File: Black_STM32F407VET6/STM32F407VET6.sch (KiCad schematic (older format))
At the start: 99 parts, among them J1 T0, J10 - HotBed +, J11 Heater0, J12 X-, J13 Y-, J14 Z-, J15 Z+, J16 USB_B, J17 LeftSpi, J18 EXTRAPINS, J19 12Vinput, J2 T1, J20 5VOut, J23 EXP2, J24 LCD2004, J25 Bottom, J26 Right, J28 LIGHTS, J29 Z, J3 TB, J30 Z, J38 X, J39 Y, J4 TC, J41 E0, J43 Heater1, J44 COM, J47 I2C, J48 SPI, J49 SPI, J5 + VIN -, J50 SDIO, J51 Servo, J52 Servo, J53 PowerSelect, J54 Power, J55 PD11, J56 Power, J6 Fan3, J7 Fan2, J8 Fan1, J9 Fan0, Q1 BCX70, Q10 BCX70, Q11 BCX70, Q12 IRLR8726PBF, Q13 IRLR8726PBF, Q14 IRLR8726PBF, Q2 BCX70, Q3 BCX70, Q4 IRLML0030TRPBF, Q5 BCX70, Q6 IRLML0030TRPBF, Q7 IRLML0030TRPBF, Q8 IRLML0030TRPBF, Q9 BCX70, SW1 Boot0, U1 LeftAnalog, U2 Left5V, U3 BuckConvertor, U5 AT24CS01-SSHM

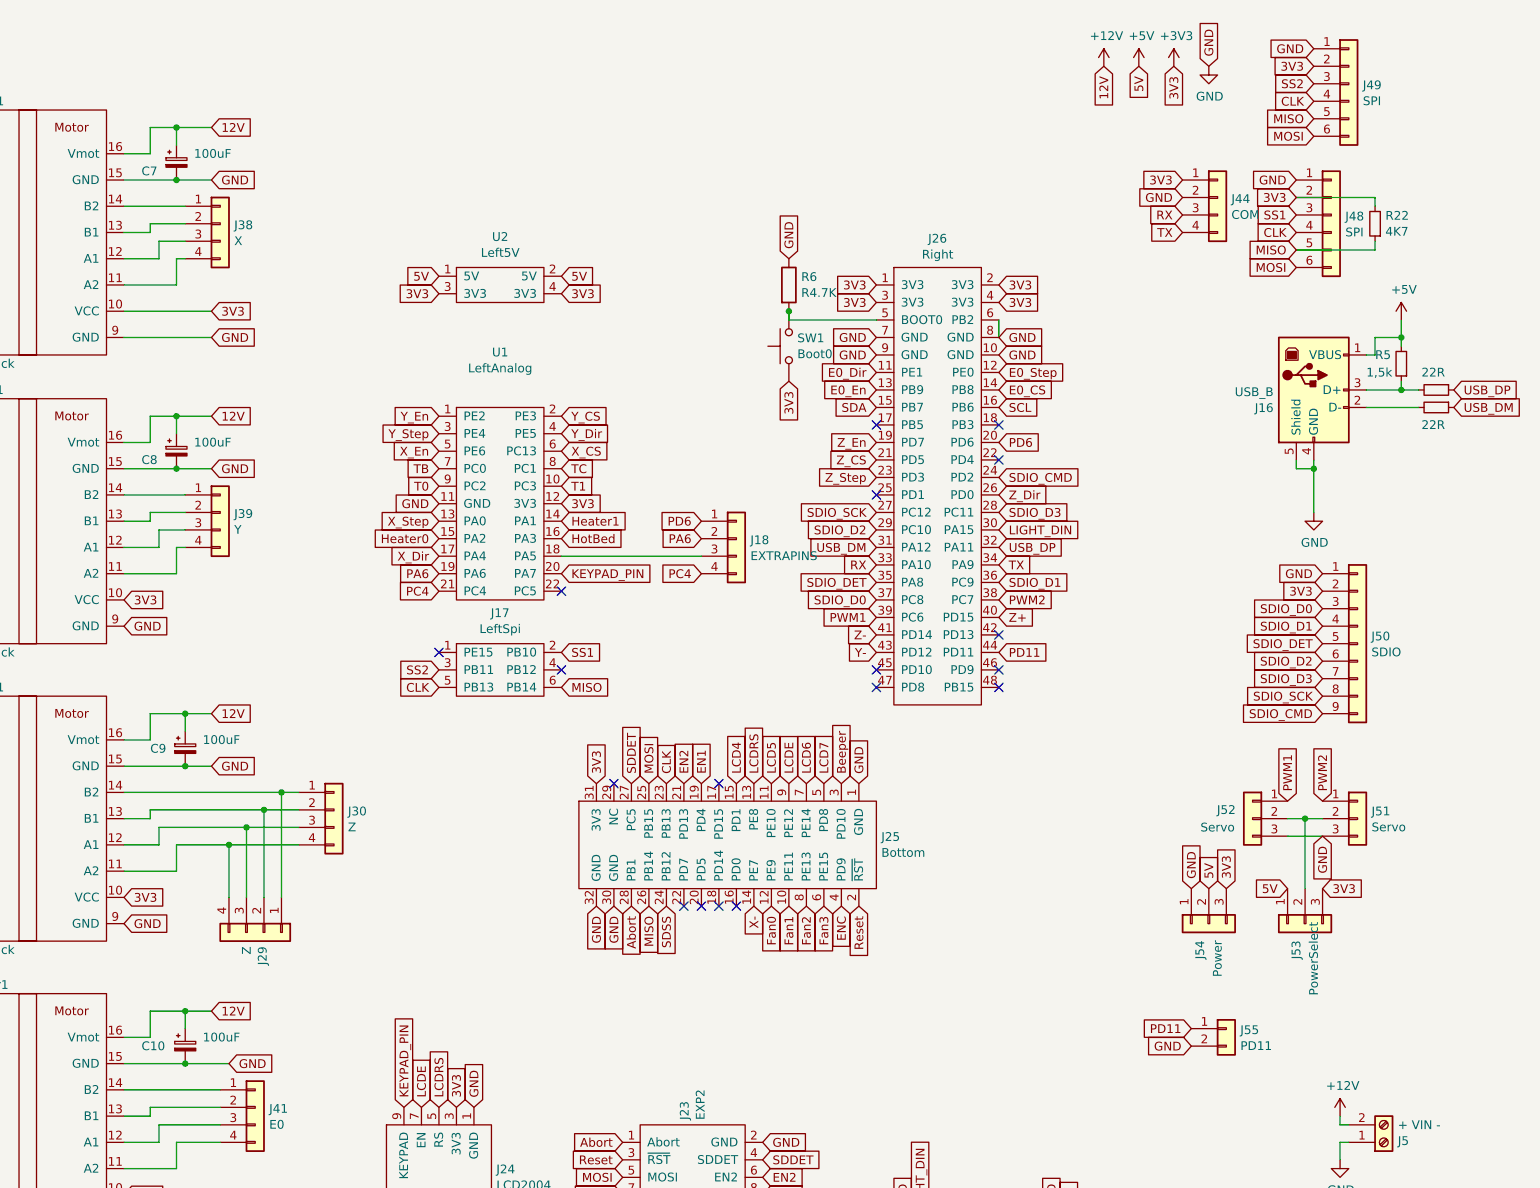
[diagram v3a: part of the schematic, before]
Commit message: Flipped back resistors to the front
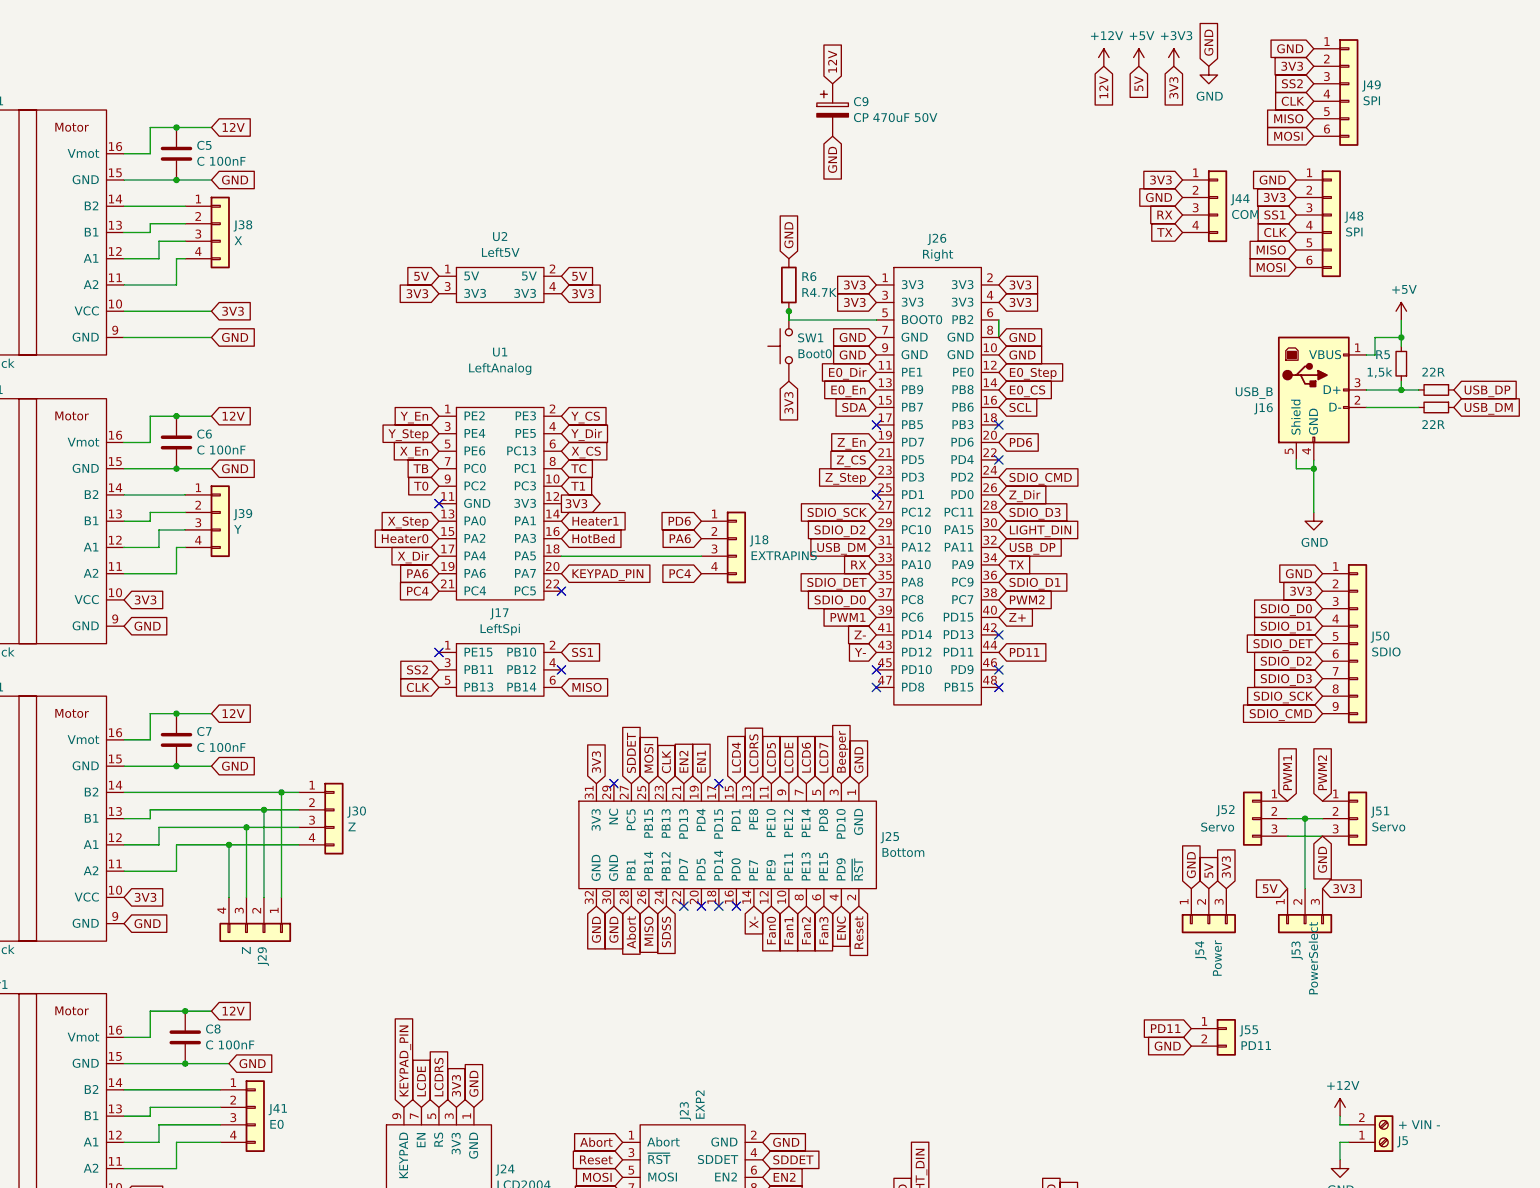
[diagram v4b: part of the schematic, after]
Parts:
- removed C10, C7, C8, C9: 100uF, Capacitor_SMD:CP_Elec_8x6.9, symbol Device:CP_Small
- removed R22: 4K7, Resistor_SMD:R_0603_1608Metric, symbol Device:R_Small
- added C5, C6, C7, C8: C 100nF, Capacitor_THT:C_Disc_D3.4mm_W2.1mm_P2.50mm, symbol Device:C
- added C9: CP 470uF 50V, Capacitor_THT:CP_Radial_D10.0mm_P5.00mm, symbol Device:CP
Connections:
- wire segments 254 -> 246
- no-connect marks 22 -> 23
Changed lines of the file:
@@
 3V3
-$Comp
-L Device:CP_Small C8
-U 1 1 5C4B7C75
-P 8300 3000
-F 0 "C8" H 8100 2950 50  0000 L CNN
-F 1 "100uF" H 8400 3050 50  0000 L CNN
-F 2 "Capacitor_SMD:CP_Elec_8x6.9" H 8300 3000 50  0001 C CNN
-F 3 "~" H 8300 3000 50  0001 C CNN
-	1    8300 3000
-	1    0    0    -1
-$EndComp
-$Comp
-L Device:CP_Small C7
-U 1 1 5C4B6EC9
-P 8300 1350
-F 0 "C7" H 8100 1300 50  0000 L CNN
-F 1 "100uF" H 8400 1400 50  0000 L CNN
-F 2 "Capacitor_SMD:CP_Elec_8x6.9" H 8300 1350 50  0001 C CNN
-F 3 "~" H 8300 1350 50  0001 C CNN
-	1    8300 1350
-	1    0    0    -1
-$EndComp
 $Comp
 L Connector_Generic:Conn_01x04 J39
@@
 Text GLabel 14700 1950 0    50   Input ~ 0
 MOSI
-Wire Wire Line
-	14700 1550 15150 1550
-Wire Wire Line
-	15150 1850 15150 1800
-Wire Wire Line
-	15150 1550 15150 1600
 Text GLabel 14100 5500 1    50   Input ~ 0
 GND
@@
 	1    15000 900
 	1    0    0    -1
-$EndComp
-Wire Wire Line
-	14700 1850 15150 1850
-$Comp
-L Device:R_Small R22
-U 1 1 5C6C524A
-P 15150 1700
-F 0 "R22" H 15091 1654 50  0000 R CNN
-F 1 "4K7" H 15091 1745 50  0000 R CNN
-F 2 "Resistor_SMD:R_0603_1608Metric" H 15150 1700 50  0001 C CNN
-F 3 "~" H 15150 1700 50  0001 C CNN
-	1    15150 1700
-	-1   0    0    1
 $EndComp
 Text GLabel 14700 1650 0    50   Input ~ 0
@@
 Wire Wire Line
 	4300 9450 4550 9450
-$Comp
-L Device:CP_Small C9
-U 1 1 5D30CFC0
-P 8350 4700
-F 0 "C9" H 8150 4700 50  0000 L CNN
-F 1 "100uF" H 8450 4750 50  0000 L CNN
-F 2 "Capacitor_SMD:CP_Elec_8x6.9" H 8350 4700 50  0001 C CNN
-F 3 "~" H 8350 4700 50  0001 C CNN
-	1    8350 4700
-	1    0    0    -1
-$EndComp
 Text GLabel 8000 5550 2    50   Input ~ 0
 3V3
@@
 	1    0    0    -1
 $EndComp
-$Comp
-L Device:CP_Small C10
-U 1 1 5C4B9316
-P 8350 6400
-F 0 "C10" H 8100 6400 50  0000 L CNN
-F 1 "100uF" H 8450 6450 50  0000 L CNN
-F 2 "Capacitor_SMD:CP_Elec_8x6.9" H 8350 6400 50  0001 C CNN
-F 3 "~" H 8350 6400 50  0001 C CNN
-	1    8350 6400
-	1    0    0    -1
-$EndComp
 Text GLabel 8000 7250 2    50   Input ~ 0
 3V3
@@
 	8150 1300 8150 1150
 Wire Wire Line
-	8150 1150 8300 1150
-Wire Wire Line
-	8300 1250 8300 1150
-Connection ~ 8300 1150
-Wire Wire Line
-	8300 1150 8500 1150
-Wire Wire Line
-	8000 1450 8300 1450
-Connection ~ 8300 1450
-Wire Wire Line
-	8300 1450 8500 1450
-Wire Wire Line
 	8000 1600 8350 1600
 Wire Wire Line
@@
 	8300 3550 8350 3550
 Wire Wire Line
-	8000 3100 8300 3100
-Wire Wire Line
 	8000 2950 8150 2950
 Wire Wire Line
-	8150 2800 8300 2800
-Wire Wire Line
-	8300 2800 8300 2900
-Wire Wire Line
 	8150 2800 8150 2950
-Wire Wire Line
-	8300 2800 8500 2800
-Connection ~ 8300 2800
-Wire Wire Line
-	8300 3100 8500 3100
-Connection ~ 8300 3100
 $Comp
 L Motor_driver:Step_stick Z_motor1
@@
 	8600 5250 9000 5250
 Wire Wire Line
-	8500 4800 8350 4800
-Connection ~ 8350 4800
-Wire Wire Line
-	8350 4800 8000 4800
-Wire Wire Line
 	8000 4650 8150 4650
 Wire Wire Line
 	8150 4650 8150 4500
-Wire Wire Line
-	8150 4500 8350 4500
-Wire Wire Line
-	8350 4600 8350 4500
-Connection ~ 8350 4500
-Wire Wire Line
-	8350 4500 8500 4500
 $Comp
 L Motor_driver:Step_stick EO_motor1
@@
 	8300 6950 8550 6950
 Wire Wire Line
-	8000 6500 8350 6500
-Wire Wire Line
 	8000 6350 8150 6350
 Wire Wire Line
 	8150 6350 8150 6200
-Connection ~ 8350 6500
-Wire Wire Line
-	8150 6200 8350 6200
-Wire Wire Line
-	8350 6300 8350 6200
-Wire Wire Line
-	8350 6500 8600 6500
-Connection ~ 8350 6200
-Wire Wire Line
-	8350 6200 8500 6200
 Wire Wire Line
 	13000 2250 13000 2350
@@
 Text GLabel 9800 4250 0    50   Input ~ 0
 SS2
-Text GLabel 10500 3300 2    50   Input ~ 0
+Text GLabel 10500 3300 2    50   Output ~ 0
 3V3
 Text GLabel 10500 3200 2    50   Input ~ 0
@@
 Text GLabel 10500 2800 2    50   Input ~ 0
 Y_CS
-Text GLabel 9800 3300 0    50   Input ~ 0
-GND
 Text GLabel 9800 3200 0    50   Input ~ 0
 T0
@@
 Text GLabel 13000 2750 2    50   Input ~ 0
 SCL
+Wire Wire Line
+	8000 6500 8350 6500
+Wire Wire Line
+	8150 6200 8350 6200
+Wire Wire Line
+	8000 4800 8300 4800
+Wire Wire Line
+	8150 4500 8300 4500
+Wire Wire Line
+	8150 2800 8300 2800
+Wire Wire Line
+	8000 3100 8300 3100
+Wire Wire Line
+	8150 1150 8300 1150
+Wire Wire Line
+	8000 1450 8300 1450
+$Comp
+L Device:CP C9
+U 1 1 5D356E9E
+P 12050 1050
+F 0 "C9" H 12168 1096 50  0000 L CNN
+F 1 "CP 470uF 50V" H 12168 1005 50  0000 L CNN
+F 2 "Capacitor_THT:CP_Radial_D10.0mm_P5.00mm" H 12088 900 50  0001 C CNN
+F 3 "~" H 12050 1050 50  0001 C CNN
+	1    12050 1050
+	1    0    0    -1
+$EndComp
+Text GLabel 12050 900  1    50   Input ~ 0
+12V
+Text GLabel 12050 1200 3    50   Input ~ 0
+GND
+$Comp
+L Device:C C6
+U 1 1 5D35A280
+P 8300 2950
+F 0 "C6" H 8415 2996 50  0000 L CNN
+F 1 "C 100nF" H 8415 2905 50  0000 L CNN
+F 2 "Capacitor_THT:C_Disc_D3.4mm_W2.1mm_P2.50mm" H 8338 2800 50  0001 C CNN
+F 3 "~" H 8300 2950 50  0001 C CNN
+	1    8300 2950
+	1    0    0    -1
+$EndComp
+Connection ~ 8300 2800
+Wire Wire Line
+	8300 2800 8500 2800
+Connection ~ 8300 3100
+Wire Wire Line
+	8300 3100 8500 3100
+$Comp
+L Device:C C5
+U 1 1 5D35C1CB
+P 8300 1300
+F 0 "C5" H 8415 1346 50  0000 L CNN
+F 1 "C 100nF" H 8415 1255 50  0000 L CNN
+F 2 "Capacitor_THT:C_Disc_D3.4mm_W2.1mm_P2.50mm" H 8338 1150 50  0001 C CNN
+F 3 "~" H 8300 1300 50  0001 C CNN
+	1    8300 1300
+	1    0    0    -1
+$EndComp
+Connection ~ 8300 1150
+Wire Wire Line
+	8300 1150 8500 1150
+Connection ~ 8300 1450
+Wire Wire Line
+	8300 1450 8500 1450
+$Comp
+L Device:C C7
+U 1 1 5D35CECB
+P 8300 4650
+F 0 "C7" H 8415 4696 50  0000 L CNN
+F 1 "C 100nF" H 8415 4605 50  0000 L CNN
+F 2 "Capacitor_THT:C_Disc_D3.4mm_W2.1mm_P2.50mm" H 8338 4500 50  0001 C CNN
+F 3 "~" H 8300 4650 50  0001 C CNN
+	1    8300 4650
+	1    0    0    -1
+$EndComp
+Connection ~ 8300 4500
+Wire Wire Line
+	8300 4500 8500 4500
+Connection ~ 8300 4800
+Wire Wire Line
+	8300 4800 8500 4800
+$Comp
+L Device:C C8
+U 1 1 5D35D96B
+P 8350 6350
+F 0 "C8" H 8465 6396 50  0000 L CNN
+F 1 "C 100nF" H 8465 6305 50  0000 L CNN
+F 2 "Capacitor_THT:C_Disc_D3.4mm_W2.1mm_P2.50mm" H 8388 6200 50  0001 C CNN
+F 3 "~" H 8350 6350 50  0001 C CNN
+	1    8350 6350
+	1    0    0    -1
+$EndComp
+Connection ~ 8350 6200
+Wire Wire Line
+	8350 6200 8500 6200
+Connection ~ 8350 6500
+Wire Wire Line
+	8350 6500 8600 6500
+NoConn ~ 9800 3300
 $EndSCHEMATC

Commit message: Added comparators to drive the mosfets.
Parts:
- removed Q1, Q10, Q11, Q2, Q3, Q5, Q9: BCX70, Package_TO_SOT_SMD:SOT-23, symbol tran:BCX70
- removed R16, R17, R26, R27, R28: 10K, Resistor_SMD:R_0603_1608Metric, symbol Device:R_Small
- removed R23, R24, R25: 100K, Resistor_SMD:R_0603_1608Metric, symbol Device:R_Small
- added R7, R8: 10K, Resistor_SMD:R_0603_1608Metric, symbol Device:R_Small
- added R9: 15K, Resistor_SMD:R_0603_1608Metric, symbol Device:R_Small
- added U4, U6: LM2901, Package_SO:SOIC-14_3.9x8.7mm_P1.27mm, symbol Comparator:LM2901
- R10, R12, R13, R14: value 100K -> 15K
- R11, R15: value 10K -> 15K
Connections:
- net labels added: Vref
- wire segments 246 -> 234

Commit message: Board layout with the opamps
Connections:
- net Fan0: now also J25.8 (PE13); no longer J25.12 (PE9)
- net Fan1: now also J25.6 (PE15); no longer J25.10 (PE11)
- net Fan2: now also J25.10 (PE11); no longer J25.8 (PE13)
- net Fan3: now also J25.12 (PE9); no longer J25.6 (PE15)
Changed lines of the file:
@@
 EESchema Schematic File Version 4
 LIBS:STM32F407VET6-cache
-EELAYER 30 0
+EELAYER 29 0
 EELAYER END
 $Descr A3 16535 11693
@@
 Text GLabel 10700 4900 1    50   Input ~ 0
 3V3
+Text GLabel 11900 5600 3    50   Input ~ 0
+Fan0
+Text GLabel 12000 5600 3    50   Input ~ 0
+Fan1
+Text GLabel 11800 5600 3    50   Input ~ 0
+Fan2
 Text GLabel 11700 5600 3    50   Input ~ 0
-Fan0
-Text GLabel 11800 5600 3    50   Input ~ 0
-Fan1
-Text GLabel 11900 5600 3    50   Input ~ 0
-Fan2
-Text GLabel 12000 5600 3    50   Input ~ 0
 Fan3
 Text GLabel 11100 5600 3    50   Input ~ 0

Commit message: Added fill zones
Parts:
- J25: symbol STM32F407VET6:Bottom -> STM32F407VET6-rescue:Bottom-STM32F407VET6
- J26: symbol STM32F407VET6:Right -> STM32F407VET6-rescue:Right-STM32F407VET6
- U2: symbol STM32F407VET6:Left5V -> STM32F407VET6-rescue:Left5V-STM32F407VET6
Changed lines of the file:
@@
 $EndComp
 $Comp
-L STM32F407VET6:Bottom J25
+L STM32F407VET6-rescue:Bottom-STM32F407VET6 J25
 U 1 1 5D30CC95
 P 11450 5250
@@
 5V
 $Comp
-L STM32F407VET6:Left5V U2
+L STM32F407VET6-rescue:Left5V-STM32F407VET6 U2
 U 1 1 5D592F71
 P 10150 2150
@@
 PD6
 $Comp
-L STM32F407VET6:Right J26
+L STM32F407VET6-rescue:Right-STM32F407VET6 J26
 U 1 1 5D30CC8F
 P 12650 3200
